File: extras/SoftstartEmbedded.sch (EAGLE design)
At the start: 27 parts, among them U1 ATTINY85

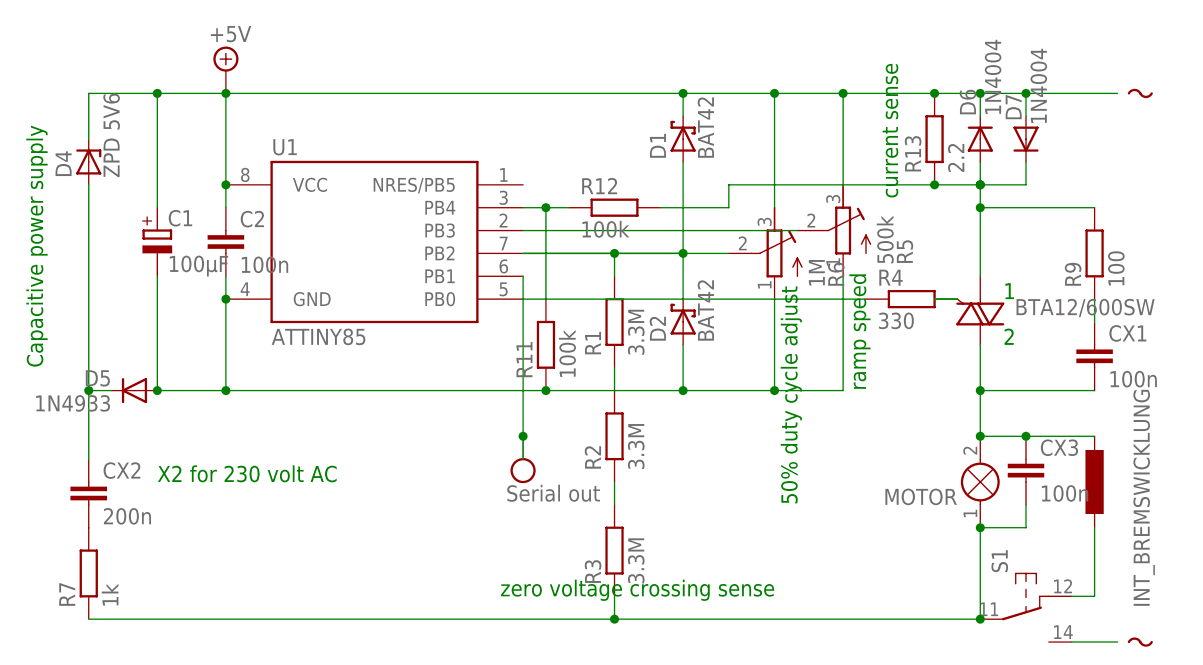
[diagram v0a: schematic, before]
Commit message: Improved load detection
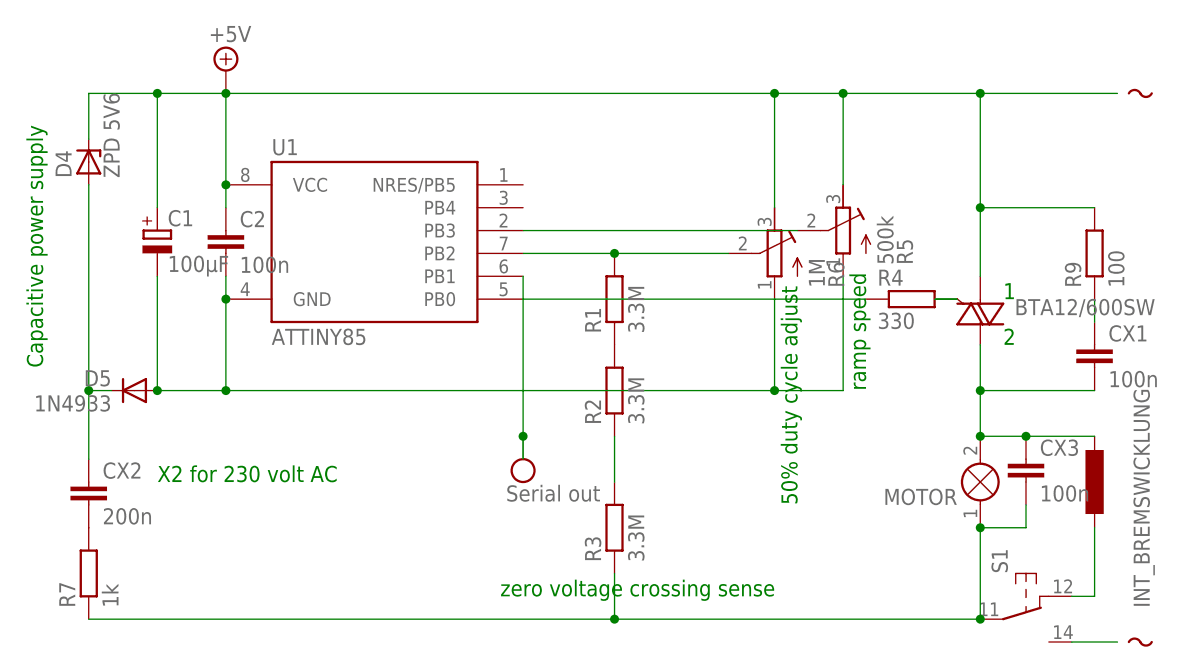
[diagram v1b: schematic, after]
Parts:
- removed D1, D2: BAT42, diode:BAT42
- removed D6, D7: 1N4004, diode:1N4004
- removed R11, R12: 100k, rcl:R-EU_0207/10
- removed R13: 2.2, rcl:R-EU_0207/10
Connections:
- removed net N$11: BTA12/600SW.A1, D6.A, D7.C, R12.2, R13.1, R9.2
- removed net N$4: R11.2, R12.1, U1.PB4
- removed net N$5: D2.C
- net +5V: now also BTA12/600SW.A1, R9.2; no longer D1.C, D6.C, D7.A, R13.2
- net N$17: no longer D2.A, R11.1
- net N$3: no longer D1.A
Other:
- note removed: "current sense"
- moved on the sheet: R1, R2, R3
